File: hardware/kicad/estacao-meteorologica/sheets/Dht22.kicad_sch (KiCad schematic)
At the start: 2 parts, among them U1 DHT22

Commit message: refatoracao: atualizacoes de hardware e falta revisao LoRa
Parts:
- added C3: 100n, Capacitor_SMD:C_0603_1608Metric, symbol Device:C
- R7: footprint Resistor_THT:R_Axial_DIN0204_L3.6mm_D1.6mm_P7.62mm_Horizontal -> Resistor_SMD:R_0603_1608Metric; Function (none) -> Pull-up do barramento DATA do DHT22; LCSC (none) -> C25804; LCSC Part (none) -> C25804; MPN (none) -> 0603WAF1002T5E; Manufacturer (none) -> UNI-ROYAL; Rating (none) -> 1%; 0.1W; 75V
- U1: footprint myLibrary:XDCR_DHT22 -> DHT22:DHT22_THT_P2.54mm_Vertical; symbol DHT22_modulo:DHT22 -> DHT22:DHT22; Availability Not in stock -> (none); CREATOR KARTHIK -> (none); Check_prices https://www.snapeda.com/parts/DHT22/Aosong+Electronics/view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 -> (none); Description_1 Capacitive-type humidity and temperature module/sensor -> (none); Function (none) -> Medição de temperatura e umidade; barramento single-wire bi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; LCSC (none) -> C83988; LCSC Part (none) -> C83988; MANUFACTURER Aosong Electronics -> (none); MAXIMUM_PACKAGE_HEIGHT 7.8 mm -> (none); MF Aosong Electronics -> (none); MP DHT22 -> (none); MPN (none) -> AM2302; Manufacturer (none) -> Aosong; Package Package -> (none); Price None -> (none); Rating (none) -> 3,3 V a 5,0 V; SIP-4; STANDARD IPC-7351B -> (none); SnapEDA_Link https://www.snapeda.com/parts/DHT22/Aosong+Electronics/view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 -> (none)
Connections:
- net GND: now also C3.2
- net +5V renamed +3V3
- net +3V3: now also C3.1
- net PA8 renamed DHT_SIG
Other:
- note added: "DHT22 local: alimentado em +3V3. R7 mantem DATA em nivel alto; o STM32 inicia a leitura puxando a linha para nivel baixo e depois a libera para leitura. C3=100n e desacoplamento local: posicionar junto aos pinos VDD/GND de U1. GND usa o simbolo global padrao do KiCad. Para sensor remoto ou cabo longo, revalidar R7, imunidade a ruido e protecao ESD antes de fabricar."

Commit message: refatoracao: lora + Verificacao projeto inteiro
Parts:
- C3: Modelo 3D (none) -> ${KICAD9_3DMODEL_DIR}/Capacitor_SMD.3dshapes/C_0603_1608Met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; Status_Ficha (none) -> Conferido no catalogo em 2026-09-24; verificar estoque ao c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
- R7: Manufacturer UNI-ROYAL -> UNI-ROYAL(Uniroyal Elec); Modelo 3D (none) -> ${KICAD9_3DMODEL_DIR}/Resistor_SMD.3dshapes/R_0603_1608Metr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; Status_Ficha (none) -> Conferido no catalogo em 2026-09-24; verificar estoque ao c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
- U1: Manufacturer Aosong -> Aosong (Guangzhou) Elec; Modelo 3D (none) -> ${KIPRJMOD}/../../libraries/DHT22/DHT22.3dshapes/DHT22_THT_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; Status_Ficha (none) -> Conferido no catalogo em 2026-09-24; verificar estoque ao c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
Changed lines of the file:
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@@
 			)
 		)
-		(property "Datasheet" "https://www.lcsc.com/product-detail/C25804.html"
-			(at 129.54 78.74 0)
-			(effects
-				(font
-					(size 1.27 1.27)
-				)
-				(hide yes)
-			)
-		)
-		(property "Description" "Resistor de filme espesso 10 kOhm, 1%, 0,1 W, encapsulamento 0603"
-			(at 129.54 78.74 0)
-			(effects
-				(font
-					(size 1.27 1.27)
-				)
-				(hide yes)
-			)
-		)
-		(property "Manufacturer" "UNI-ROYAL"
+		(property "Datasheet" "https://www.lcsc.com/datasheet/lcsc_datasheet_2206010045_UNI-ROYAL-Uniroyal-Elec-0603WAF1002T5E_C25804.pdf"
+			(at 129.54 78.74 0)
+			(effects
+				(font
+					(size 1.27 1.27)
+				)
+				(hide yes)
+			)
+		)
+		(property "Description" "Resistor SMD 10 kohm, 1%, 0,1 W, 0603"
+			(at 129.54 78.74 0)
+			(effects
+				(font
+					(size 1.27 1.27)
+				)
+				(hide yes)
+			)
+		)
+		(property "Manufacturer" "UNI-ROYAL(Uniroyal Elec)"
 			(at 129.54 78.74 0)
 			(effects
@@
 				(font
 					(size 1 1)
+				)
+				(hide yes)
+			)
+		)
+		(property "Modelo 3D" "${KICAD9_3DMODEL_DIR}/Resistor_SMD.3dshapes/R_0603_1608Metric.step"
+			(at 129.54 78.74 0)
+			(effects
+				(font
+					(size 1.27 1.27)
+				)
+				(hide yes)
+			)
+		)
+		(property "Status_Ficha" "Conferido no catalogo em 2026-09-24; verificar estoque ao comprar"
+			(at 129.54 78.74 0)
+			(effects
+				(font
+					(size 1.27 1.27)
+				)
+				(hide yes)
+			)
+		)
+		(property "CREATOR" ""
+			(at 129.54 78.74 90)
+			(effects
+				(font
+					(size 1.27 1.27)
+				)
+				(hide yes)
+			)
+		)
+		(property "VERIFIER" ""
+			(at 129.54 78.74 90)
+			(effects
+				(font
+					(size 1.27 1.27)
 				)
 				(hide yes)
@@
 			)
 		)
-		(property "Datasheet" "https://www.lcsc.com/product-detail/C83988.html"
-			(at 133.35 95.25 0)
-			(effects
-				(font
-					(size 1.27 1.27)
-				)
-				(hide yes)
-			)
-		)
-		(property "Description" "Sensor digital de temperatura e umidade DHT22/AM2302; SIP-4; 3,3 V a 5,0 V"
-			(at 133.35 95.25 0)
-			(effects
-				(font
-					(size 1.27 1.27)
-				)
-				(hide yes)
-			)
-		)
-		(property "Manufacturer" "Aosong"
+		(property "Datasheet" "https://www.lcsc.com/datasheet/lcsc_datasheet_1810051021_Aosong--Guangzhou-Elec-AM2302_C83988.pdf"
+			(at 133.35 95.25 0)
+			(effects
+				(font
+					(size 1.27 1.27)
+				)
+				(hide yes)
+			)
+		)
+		(property "Description" "0%RH~99.9%RH 16bit 3.3V~5.5V 300uA Single-bus ±0.5℃ ±2%RH SIP-4 Temperature and Humidity Sensor RoHS"
+			(at 133.35 95.25 0)
+			(effects
+				(font
+					(size 1.27 1.27)
+				)
+				(hide yes)
+			)
+		)
+		(property "Manufacturer" "Aosong (Guangzhou) Elec"
 			(at 133.35 95.25 0)
 			(effects
@@
 				)
 				(justify bottom)
+				(hide yes)
+			)
+		)
+		(property "Modelo 3D" "${KIPRJMOD}/../../libraries/DHT22/DHT22.3dshapes/DHT22_THT_P2.54mm_Vertical.wrl"
+			(at 133.35 95.25 0)
+			(effects
+				(font
+					(size 1.27 1.27)
+				)
+				(hide yes)
+			)
+		)
+		(property "Status_Ficha" "Conferido no catalogo em 2026-09-24; verificar estoque ao comprar"
+			(at 133.35 95.25 0)
+			(effects
+				(font
+					(size 1.27 1.27)
+				)
+				(hide yes)
+			)
+		)
+		(property "CREATOR" ""
+			(at 133.35 95.25 90)
+			(effects
+				(font
+					(size 1.27 1.27)
+				)
+				(hide yes)
+			)
+		)
+		(property "VERIFIER" ""
+			(at 133.35 95.25 90)
+			(effects
+				(font
+					(size 1.27 1.27)
+				)
 				(hide yes)
 			)
@@
 			)
 		)
-		(property "Datasheet" "https://www.lcsc.com/product-detail/C14663.html"
-			(at 119.38 86.36 0)
-			(effects
-				(font
-					(size 1 1)
-				)
-				(hide yes)
-			)
-		)
-		(property "Description" "Capacitor ceramico 100 nF, 10%, 50 V, X7R, encapsulamento 0603"
+		(property "Datasheet" "https://www.lcsc.com/datasheet/lcsc_datasheet_2211101700_YAGEO-CC0603KRX7R9BB104_C14663.pdf"
+			(at 119.38 86.36 0)
+			(effects
+				(font
+					(size 1 1)
+				)
+				(hide yes)
+			)
+		)
+		(property "Description" "Capacitor ceramico 100 nF, 50 V, X7R, 10%, 0603"
 			(at 119.38 86.36 0)
 			(effects
@@
 				)
 				(hide yes)
+			)
+		)
+		(property "Modelo 3D" "${KICAD9_3DMODEL_DIR}/Capacitor_SMD.3dshapes/C_0603_1608Metric.step"
+			(at 119.38 86.36 0)
+			(effects
+				(font
+					(size 1.27 1.27)
+				)
+				(hide yes)
+			)
+		)
+		(property "Status_Ficha" "Conferido no catalogo em 2026-09-24; verificar estoque ao comprar"
+			(at 119.38 86.36 0)
+			(effects
+				(font
+					(size 1.27 1.27)
+				)
+				(hide yes)
+			)
+		)
+		(property "CREATOR" ""
+			(at 119.38 86.36 0)
+			(effects
+				(font
+					(size 1.27 1.27)
+				)
+				(hide yes)
+			)
+		)
+		(property "VERIFIER" ""
+			(at 119.38 86.36 0)
+			(effects
+				(font
+					(size 1.27 1.27)
+				)
+				(hide yes)

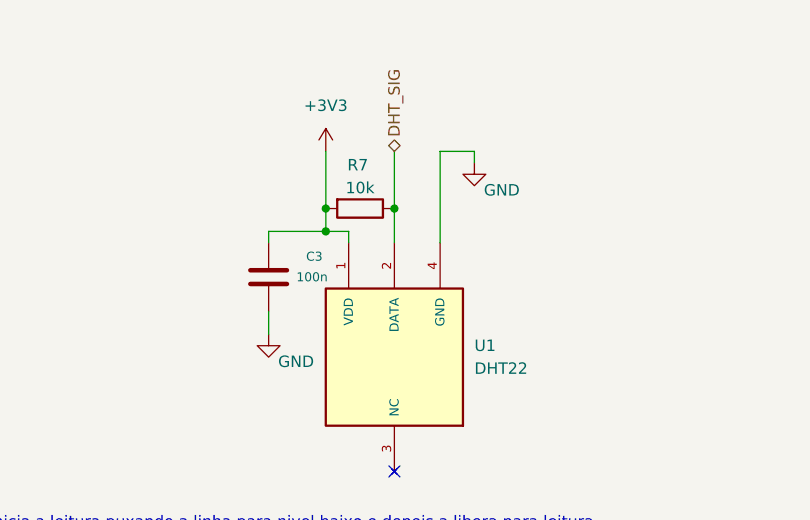
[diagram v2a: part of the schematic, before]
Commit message: Padronizacao de nomes e numero de componentes
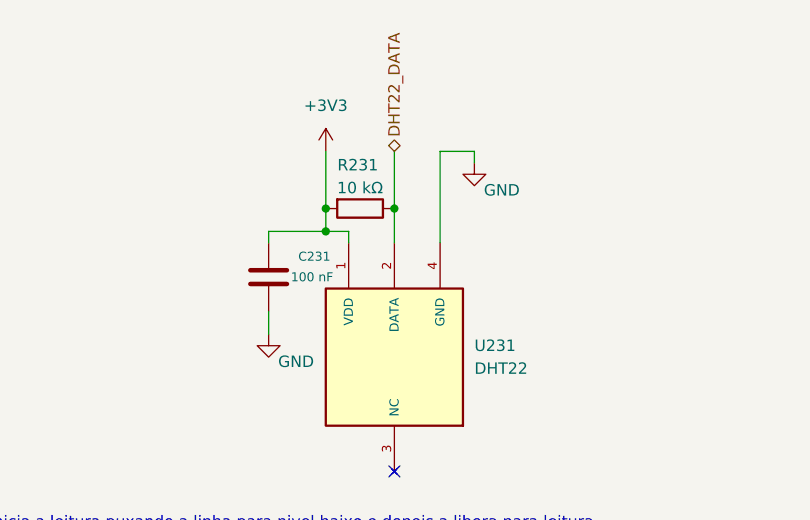
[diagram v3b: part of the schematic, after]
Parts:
- C231: renamed from C3; value 100n -> 100 nF; Assembly (none) -> SMT; LCSC Part C14663 -> (none); Modelo 3D ${KICAD9_3DMODEL_DIR}/Capacitor_SMD.3dshapes/C_0603_1608Met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 -> (none); Rating 10%; 50V; X7R -> (none); Specification (none) -> 10%; 50V; X7R; Status_Ficha Conferido no catalogo em 2026-09-24; verificar estoque ao c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 -> (none); Verification (none) -> Conferido no catalogo em 2026-09-24; verificar estoque ao c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
- R231: renamed from R7; value 10k -> 10 kΩ; Assembly (none) -> SMT; LCSC Part C25804 -> (none); Modelo 3D ${KICAD9_3DMODEL_DIR}/Resistor_SMD.3dshapes/R_0603_1608Metr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 -> (none); Rating 1%; 0.1W; 75V -> (none); Specification (none) -> 1%; 0.1W; 75V; Status_Ficha Conferido no catalogo em 2026-09-24; verificar estoque ao c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 -> (none); Verification (none) -> Conferido no catalogo em 2026-09-24; verificar estoque ao c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
- U231: renamed from U1; Assembly (none) -> THT — montagem manual; LCSC Part C83988 -> (none); Modelo 3D ${KIPRJMOD}/../../libraries/DHT22/DHT22.3dshapes/DHT22_THT_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 -> (none); Rating 3,3 V a 5,0 V; SIP-4 -> (none); Specification (none) -> 3,3 V a 5,0 V; SIP-4; Status_Ficha Conferido no catalogo em 2026-09-24; verificar estoque ao c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 -> (none); Verification (none) -> Conferido no catalogo em 2026-09-24; verificar estoque ao c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
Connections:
- net DHT_SIG renamed DHT22_DATA
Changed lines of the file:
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@@
 		)
 	)
-	(hierarchical_label "DHT_SIG"
+	(hierarchical_label "DHT22_DATA"
 		(shape bidirectional)
 		(at 133.35 72.39 90)
@@
 		(on_board yes)
 		(dnp no)
-		(property "Reference" "R7"
+		(property "Reference" "R231"
 			(at 129.286 73.914 90)
 			(effects
@@
 			)
 		)
-		(property "Value" "10k"
+		(property "Value" "10 kΩ"
 			(at 129.54 76.454 90)
 			(effects
@@
 			)
 		)
-		(property "LCSC Part" "C25804"
-			(at 129.54 78.74 0)
-			(effects
-				(font
-					(size 1 1)
-				)
-				(hide yes)
-			)
-		)
-		(property "Rating" "1%; 0.1W; 75V"
+		(property "Specification" "1%; 0.1W; 75V"
 			(at 129.54 78.74 0)
 			(effects
@@
 			)
 		)
-		(property "Modelo 3D" "${KICAD9_3DMODEL_DIR}/Resistor_SMD.3dshapes/R_0603_1608Metric.step"
-			(at 129.54 78.74 0)
-			(effects
-				(font
-					(size 1.27 1.27)
-				)
-				(hide yes)
-			)
-		)
-		(property "Status_Ficha" "Conferido no catalogo em 2026-09-24; verificar estoque ao comprar"
-			(at 129.54 78.74 0)
-			(effects
-				(font
-					(size 1.27 1.27)
-				)
-				(hide yes)
-			)
-		)
-		(property "CREATOR" ""
-			(at 129.54 78.74 90)
-			(effects
-				(font
-					(size 1.27 1.27)
-				)
-				(hide yes)
-			)
-		)
-		(property "VERIFIER" ""
-			(at 129.54 78.74 90)
+		(property "Verification" "Conferido no catalogo em 2026-09-24; verificar estoque ao comprar"
+			(at 129.54 78.74 0)
 			(effects
 				(font
@@
 			(project "esquematico_V4"
 				(path "/0c305a6e-f9cd-49a1-b146-c2956e5469b6/34d78a87-9b09-4795-98a5-fe6ea1a123f9"
-					(reference "R7")
+					(reference "R231")
 					(unit 1)
 				)
+			)
+		)
+		(property "Assembly" "SMT"
+			(at 0 0 0)
+			(effects
+				(font (size 1.27 1.27))
+				(hide yes)
 			)
 		)
@@
 		(dnp no)
 		(fields_autoplaced yes)
-		(property "Reference" "U1"
+		(property "Reference" "U231"
 			(at 142.24 93.9799 90)
 			(effects
@@
 			)
 		)
-		(property "LCSC Part" "C83988"
+		(property "Specification" "3,3 V a 5,0 V; SIP-4"
 			(at 133.35 95.25 0)
 			(effects
@@
 			)
 		)
-		(property "Rating" "3,3 V a 5,0 V; SIP-4"
+		(property "Function" "Medição de temperatura e umidade; barramento single-wire bidirecional"
 			(at 133.35 95.25 0)
 			(effects
@@
 			)
 		)
-		(property "Function" "Medição de temperatura e umidade; barramento single-wire bidirecional"
-			(at 133.35 95.25 0)
-			(effects
-				(font
-					(size 1.27 1.27)
-				)
-				(justify bottom)
-				(hide yes)
-			)
-		)
-		(property "Modelo 3D" "${KIPRJMOD}/../../libraries/DHT22/DHT22.3dshapes/DHT22_THT_P2.54mm_Vertical.wrl"
-			(at 133.35 95.25 0)
-			(effects
-				(font
-					(size 1.27 1.27)
-				)
-				(hide yes)
-			)
-		)
-		(property "Status_Ficha" "Conferido no catalogo em 2026-09-24; verificar estoque ao comprar"
-			(at 133.35 95.25 0)
-			(effects
-				(font
-					(size 1.27 1.27)
-				)
-				(hide yes)
-			)
-		)
-		(property "CREATOR" ""
-			(at 133.35 95.25 90)
-			(effects
-				(font
-					(size 1.27 1.27)
-				)
-				(hide yes)
-			)
-		)
-		(property "VERIFIER" ""
-			(at 133.35 95.25 90)
+		(property "Verification" "Conferido no catalogo em 2026-09-24; verificar estoque ao comprar"
+			(at 133.35 95.25 0)
 			(effects
 				(font
@@
 			(project "esquematico_V4"
 				(path "/0c305a6e-f9cd-49a1-b146-c2956e5469b6/34d78a87-9b09-4795-98a5-fe6ea1a123f9"
-					(reference "U1")
+					(reference "U231")
 					(unit 1)
 				)
+			)
+		)
+		(property "Assembly" "THT — montagem manual"
+			(at 0 0 0)
+			(effects
+				(font (size 1.27 1.27))
+				(hide yes)
 			)
 		)
@@
 		(on_board yes)
 		(dnp no)
-		(property "Reference" "C3"
+		(property "Reference" "C231"
 			(at 124.46 84.074 0)
 			(effects
@@
 			)
 		)
-		(property "Value" "100n"
+		(property "Value" "100 nF"
 			(at 124.206 86.36 0)
 			(effects
@@
 			)
 		)
-		(property "LCSC Part" "C14663"
-			(at 119.38 86.36 0)
-			(effects
-				(font
-					(size 1 1)
-				)
-				(hide yes)
-			)
-		)
-		(property "Rating" "10%; 50V; X7R"
+		(property "Specification" "10%; 50V; X7R"
 			(at 119.38 86.36 0)
 			(effects
@@
 			)
 		)
-		(property "Modelo 3D" "${KICAD9_3DMODEL_DIR}/Capacitor_SMD.3dshapes/C_0603_1608Metric.step"
-			(at 119.38 86.36 0)
-			(effects
-				(font
-					(size 1.27 1.27)
-				)
-				(hide yes)
-			)
-		)
-		(property "Status_Ficha" "Conferido no catalogo em 2026-09-24; verificar estoque ao comprar"
-			(at 119.38 86.36 0)
-			(effects
-				(font
-					(size 1.27 1.27)
-				)
-				(hide yes)
-			)
-		)
-		(property "CREATOR" ""
-			(at 119.38 86.36 0)
-			(effects
-				(font
-					(size 1.27 1.27)
-				)
-				(hide yes)
-			)
-		)
-		(property "VERIFIER" ""
+		(property "Verification" "Conferido no catalogo em 2026-09-24; verificar estoque ao comprar"
 			(at 119.38 86.36 0)
 			(effects
@@
 			(project "estacao-meteorologica"
 				(path "/0c305a6e-f9cd-49a1-b146-c2956e5469b6/34d78a87-9b09-4795-98a5-fe6ea1a123f9"
-					(reference "C3")
+					(reference "C231")
 					(unit 1)
 				)
 			)
 		)
+		(property "Assembly" "SMT"
+			(at 0 0 0)
+			(effects
+				(font (size 1.27 1.27))
+				(hide yes)
+			)
+		)

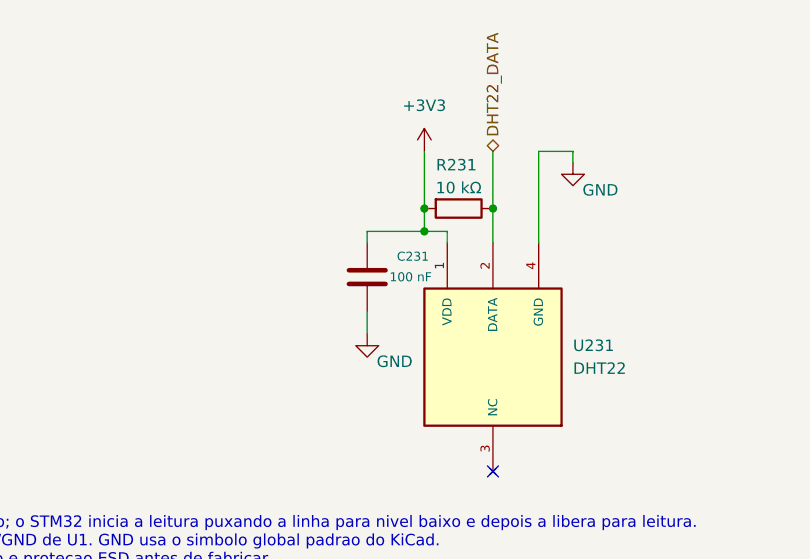
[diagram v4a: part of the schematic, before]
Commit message: Add test points necessarios para debug
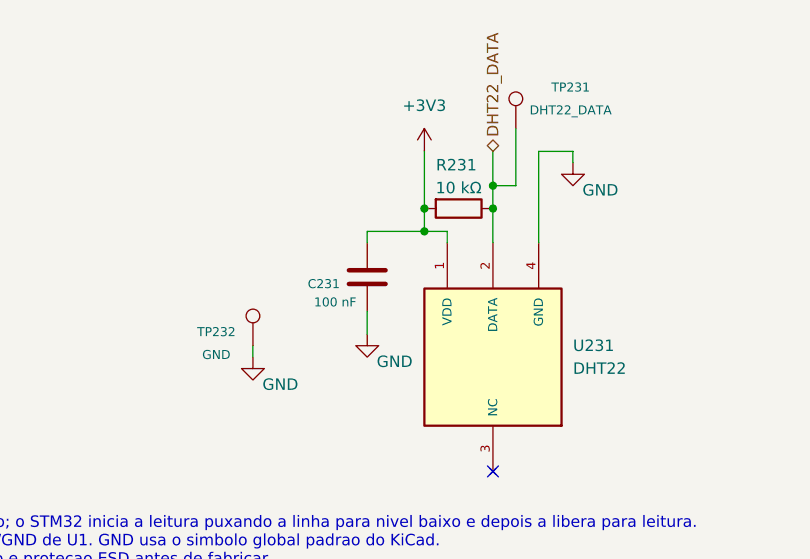
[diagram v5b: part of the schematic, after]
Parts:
- added TP231: DHT22_DATA, TestPoint:TestPoint_Pad_D1.0mm, symbol Connector:TestPoint
- added TP232: GND, TestPoint:TestPoint_Pad_D1.0mm, symbol Connector:TestPoint
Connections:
- net DHT22_DATA: now also TP231.1
- net GND: now also TP232.1
